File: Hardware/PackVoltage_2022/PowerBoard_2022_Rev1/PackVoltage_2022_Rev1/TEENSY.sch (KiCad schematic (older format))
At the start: 8 parts

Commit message: Back to TEENSY
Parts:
- removed U? (x8): TM4C129E_Launchpad, symbol MRDT_Shields:TM4C129E_Launchpad
- added U?: Teensy4.1_DEV-16771, MODULE_DEV-16771, symbol MRDT_Shields:Teensy4.1_DEV-16771
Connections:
- net labels added: Current_Sensor_Spare
- net labels removed: Current_Sensor_AuxAct, Current_Sensor_AuxLog, Current_Sensor_BBB, Current_Sensor_Cam1, Current_Sensor_Cam2, Current_Sensor_Drive, Current_Sensor_GimAct, Current_Sensor_GimLog, Current_Sensor_Multi, Current_Sensor_Nav, Current_Sensor_NetSwitch, Current_Sensor_SciAct, Driver_AuxAct, Driver_AuxLog, Driver_BBB, Driver_Cam1, Driver_Cam2, Driver_Drive, Driver_GimAct, Driver_Multi, Driver_Nav, Driver_NetSwitch, Driver_SciAct, Driver_SciLog
- wire segments 43 -> 22
- no-connect marks 34 -> 38

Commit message: Organizing stuff
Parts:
- U19: renamed from U?; footprint MODULE_DEV-16771 -> MRDT_Shields:MODULE_DEV-16771
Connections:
- no-connect marks 38 -> 39
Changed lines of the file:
@@
 Current_Sensor_M5
 $Comp
-L MRDT_Shields:Teensy4.1_DEV-16771 U?
+L MRDT_Shields:Teensy4.1_DEV-16771 U19
 U 1 1 62368E05
 P 5600 3550
-F 0 "U?" H 5600 5717 50  0000 C CNN
+F 0 "U19" H 5600 5717 50  0000 C CNN
 F 1 "Teensy4.1_DEV-16771" H 5600 5626 50  0000 C CNN
-F 2 "MODULE_DEV-16771" H 7700 3250 50  0001 L BNN
+F 2 "MRDT_Shields:MODULE_DEV-16771" H 7700 3250 50  0001 L BNN
 F 3 "" H 5600 3550 50  0001 L BNN
 F 4 "Manufacturer recommendations" H 7700 3000 50  0001 L BNN "STANDARD"
@@
 	6550 1750 6550 1550
 $Comp
-L power:+3.3V #PWR?
+L power:+3.3V #PWR0144
 U 1 1 623850B6
 P 6550 1550
-F 0 "#PWR?" H 6550 1400 50  0001 C CNN
+F 0 "#PWR0144" H 6550 1400 50  0001 C CNN
 F 1 "+3.3V" H 6565 1723 50  0000 C CNN
 F 2 "" H 6550 1550 50  0001 C CNN
@@
 	6500 5450 6500 5550
 $Comp
-L power:GND #PWR?
+L power:GND #PWR0145
 U 1 1 623DD9ED
 P 6500 5550
-F 0 "#PWR?" H 6500 5300 50  0001 C CNN
+F 0 "#PWR0145" H 6500 5300 50  0001 C CNN
 F 1 "GND" H 6505 5377 50  0000 C CNN
 F 2 "" H 6500 5550 50  0001 C CNN
@@
 	1    0    0    -1
 $EndComp
+NoConn ~ 6400 1650
 $EndSCHEMATC

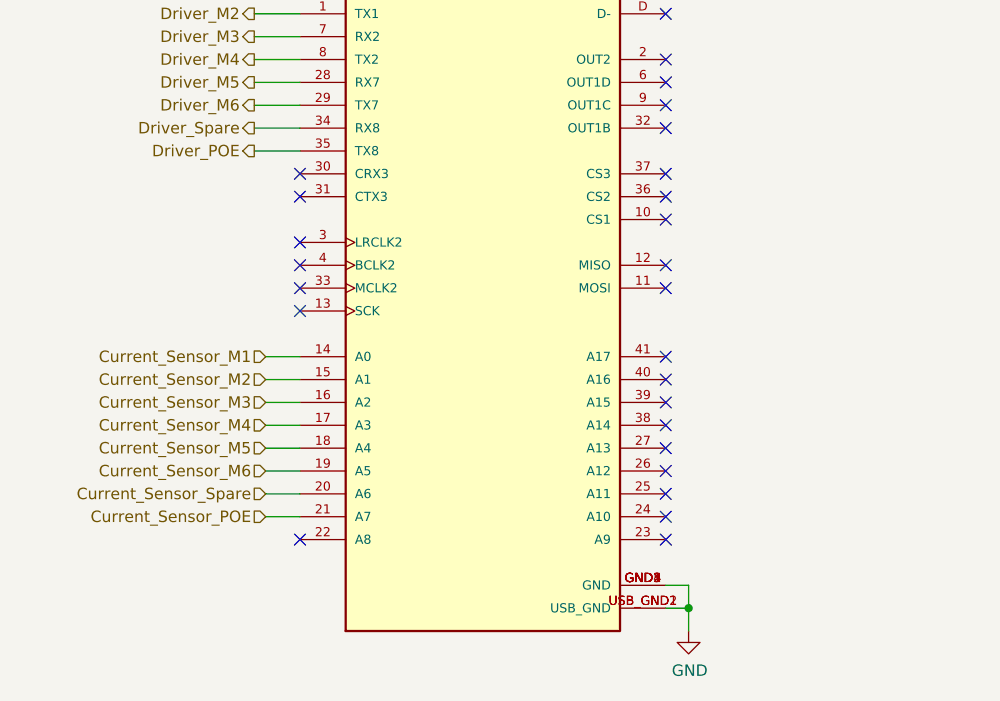
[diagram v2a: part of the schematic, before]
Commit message: added molex and fixed teensy
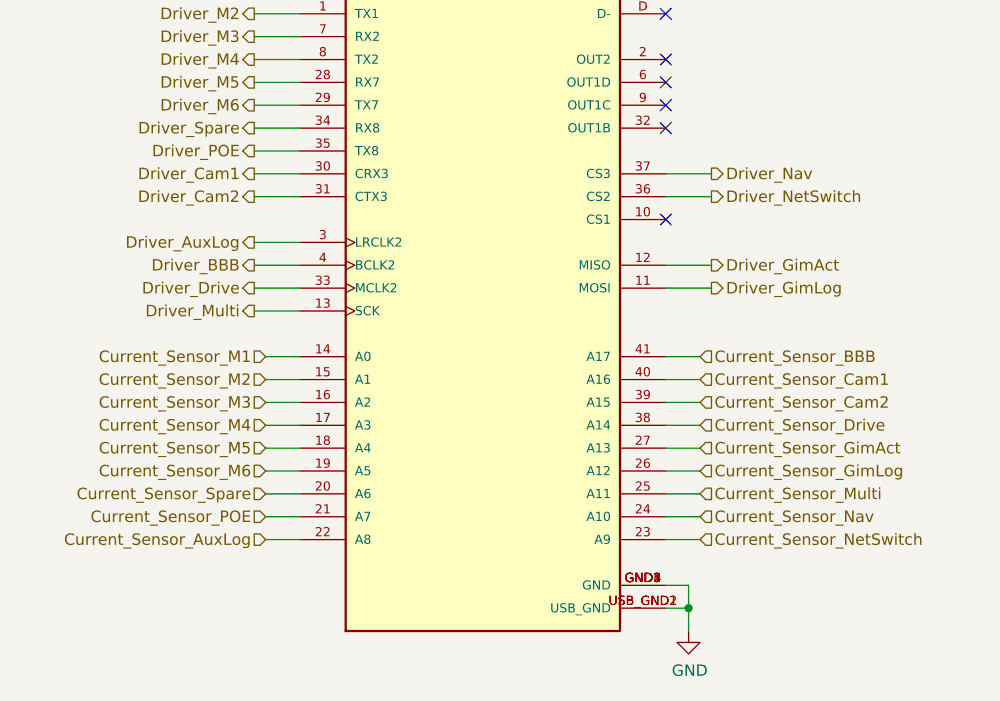
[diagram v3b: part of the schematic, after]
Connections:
- net Driver_GimLog: now reaches U19.11 (MOSI)
- net Driver_GimAct: now reaches U19.12 (MISO)
- net Driver_Multi: now reaches U19.13 (SCK)
- net Current_Sensor_AuxLog: now reaches U19.22 (A8)
- net Current_Sensor_NetSwitch: now reaches U19.23 (A9)
- net Current_Sensor_Nav: now reaches U19.24 (A10)
- net Current_Sensor_Multi: now reaches U19.25 (A11)
- net Current_Sensor_GimLog: now reaches U19.26 (A12)
- net Current_Sensor_GimAct: now reaches U19.27 (A13)
- net Driver_AuxLog: now reaches U19.3 (LRCLK2)
- net Driver_Cam1: now reaches U19.30 (CRX3)
- net Driver_Cam2: now reaches U19.31 (CTX3)
- net Driver_Drive: now reaches U19.33 (MCLK2)
- net Driver_NetSwitch: now reaches U19.36 (CS2)
- net Driver_Nav: now reaches U19.37 (CS3)
- net Current_Sensor_Drive: now reaches U19.38 (A14)
- net Current_Sensor_Cam2: now reaches U19.39 (A15)
- net Driver_BBB: now reaches U19.4 (BCLK2)
- net Current_Sensor_Cam1: now reaches U19.40 (A16)
- net Current_Sensor_BBB: now reaches U19.41 (A17)
- no-connect marks 39 -> 19
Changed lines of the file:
@@
 	1    0    0    -1
 $EndComp
-NoConn ~ 4800 5150
-NoConn ~ 6400 5150
-NoConn ~ 6400 5050
-NoConn ~ 6400 4950
-NoConn ~ 6400 4850
-NoConn ~ 6400 4750
-NoConn ~ 6400 4650
-NoConn ~ 6400 4550
-NoConn ~ 6400 4450
-NoConn ~ 6400 4350
-NoConn ~ 6400 4050
-NoConn ~ 6400 3950
-NoConn ~ 6400 3750
-NoConn ~ 6400 3650
-NoConn ~ 6400 3550
 NoConn ~ 6400 3350
 NoConn ~ 6400 3250
@@
 Wire Wire Line
 	4600 3450 4800 3450
-NoConn ~ 4800 3550
-NoConn ~ 4800 3650
-NoConn ~ 4800 3850
-NoConn ~ 4800 3950
-NoConn ~ 4800 4050
-NoConn ~ 4800 4150
 Wire Wire Line
 	6400 5350 6500 5350
@@
 $EndComp
 NoConn ~ 6400 1650
+Text HLabel 4650 5150 0    50   Input ~ 0
+Current_Sensor_AuxLog
+Wire Wire Line
+	4650 5150 4800 5150
+Text HLabel 6550 4350 2    50   Input ~ 0
+Current_Sensor_BBB
+Wire Wire Line
+	6550 4350 6400 4350
+Text HLabel 6550 4450 2    50   Input ~ 0
+Current_Sensor_Cam1
+Wire Wire Line
+	6550 4450 6400 4450
+Text HLabel 6550 4550 2    50   Input ~ 0
+Current_Sensor_Cam2
+Wire Wire Line
+	6550 4550 6400 4550
+Text HLabel 6550 4650 2    50   Input ~ 0
+Current_Sensor_Drive
+Wire Wire Line
+	6550 4650 6400 4650
+Text HLabel 6550 4750 2    50   Input ~ 0
+Current_Sensor_GimAct
+Wire Wire Line
+	6550 4750 6400 4750
+Text HLabel 6550 4850 2    50   Input ~ 0
+Current_Sensor_GimLog
+Wire Wire Line
+	6550 4850 6400 4850
+Text HLabel 6550 4950 2    50   Input ~ 0
+Current_Sensor_Multi
+Wire Wire Line
+	6550 4950 6400 4950
+Text HLabel 6550 5050 2    50   Input ~ 0
+Current_Sensor_Nav
+Wire Wire Line
+	6550 5050 6400 5050
+Text HLabel 6550 5150 2    50   Input ~ 0
+Current_Sensor_NetSwitch
+Wire Wire Line
+	6550 5150 6400 5150
+Text HLabel 4600 3550 0    50   Output ~ 0
+Driver_Cam1
+Wire Wire Line
+	4600 3550 4800 3550
+Text HLabel 4600 3650 0    50   Output ~ 0
+Driver_Cam2
+Wire Wire Line
+	4600 3650 4800 3650
+Text HLabel 4600 3850 0    50   Output ~ 0
+Driver_AuxLog
+Wire Wire Line
+	4600 3850 4800 3850
+Text HLabel 4600 3950 0    50   Output ~ 0
+Driver_BBB
+Wire Wire Line
+	4600 3950 4800 3950
+Text HLabel 4600 4050 0    50   Output ~ 0
+Driver_Drive
+Wire Wire Line
+	4600 4050 4800 4050
+Text HLabel 4600 4150 0    50   Output ~ 0
+Driver_Multi
+Wire Wire Line
+	4600 4150 4800 4150
+Text HLabel 6600 3950 2    50   Output ~ 0
+Driver_GimAct
+Wire Wire Line
+	6600 3950 6400 3950
+Text HLabel 6600 4050 2    50   Output ~ 0
+Driver_GimLog
+Wire Wire Line
+	6600 4050 6400 4050
+Text HLabel 6600 3550 2    50   Output ~ 0
+Driver_Nav
+Wire Wire Line
+	6600 3550 6400 3550
+Text HLabel 6600 3650 2    50   Output ~ 0
+Driver_NetSwitch
+Wire Wire Line
+	6600 3650 6400 3650
+NoConn ~ 6400 3750
 $EndSCHEMATC

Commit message: Somewhat completed schematic
did stuff
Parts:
- added C?: 0.1 uF, symbol Device:CP1
- added Conn?: Molex_uF_D_06, MRDT_Connectors:MOLEX_uF_D_06_Horizontal, symbol MRDT_Connectors:Molex_uF_D_06
- added J?: RJ45_LED_Shielded, symbol Connector:RJ45_LED_Shielded
- U19: symbol MRDT_Shields:Teensy4.1_DEV-16771 -> PackVoltage_2022_Rev1-rescue:Teensy4.1_DEV-16771-MRDT_Shields
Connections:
- net Current_Sensor_GimAct is gone; now on net Current_Sensor_Drive: U19.27 (A13)
- net Current_Sensor_BBB: now also U19.40 (A16); no longer U19.41 (A17)
- net Current_Sensor_Cam1: now also U19.39 (A15); no longer U19.40 (A16)
- net Current_Sensor_Cam2: now also U19.38 (A14); no longer U19.39 (A15)
- net Current_Sensor_Drive: no longer U19.38 (A14)
- net GND: now also J?.SH
- net Driver_AuxAct: now reaches U19.10 (CS1)
- net Current_Sensor_GimLog renamed Current_Sensor_Gim
- net Driver_GimAct: no longer names the net of U19.12 (MISO)
- net Driver_GimLog renamed Driver_Gim
- new net: Conn?.1, J?.1
- new net: Conn?.4, J?.10
- new net: C?.1, J?.2, J?.5
- new net: Conn?.2, J?.3
- new net: Conn?.6, J?.4
- new net: Conn?.5, J?.6
- new net: C?.2, Conn?.3, J?.8, J?.9
- new net Current_Sensor_AuxAct: U19.41 (A17)
- no-connect marks 19 -> 22
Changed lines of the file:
@@
 Current_Sensor_M5
 $Comp
-L MRDT_Shields:Teensy4.1_DEV-16771 U19
+L PackVoltage_2022_Rev1-rescue:Teensy4.1_DEV-16771-MRDT_Shields U19
 U 1 1 62368E05
 P 5600 3550
@@
 NoConn ~ 6400 2850
 NoConn ~ 6400 2750
-NoConn ~ 6400 2550
-NoConn ~ 6400 2450
-NoConn ~ 6400 2350
-NoConn ~ 6400 2250
-NoConn ~ 6400 2150
 NoConn ~ 6400 1850
 NoConn ~ 6400 1950
@@
 Wire Wire Line
 	4650 5150 4800 5150
-Text HLabel 6550 4350 2    50   Input ~ 0
+Text HLabel 6550 4450 2    50   Input ~ 0
 Current_Sensor_BBB
 Wire Wire Line
 	6550 4350 6400 4350
-Text HLabel 6550 4450 2    50   Input ~ 0
+Text HLabel 6550 4550 2    50   Input ~ 0
 Current_Sensor_Cam1
 Wire Wire Line
 	6550 4450 6400 4450
-Text HLabel 6550 4550 2    50   Input ~ 0
+Text HLabel 6550 4650 2    50   Input ~ 0
 Current_Sensor_Cam2
 Wire Wire Line
 	6550 4550 6400 4550
-Text HLabel 6550 4650 2    50   Input ~ 0
+Text HLabel 6550 4750 2    50   Input ~ 0
 Current_Sensor_Drive
 Wire Wire Line
 	6550 4650 6400 4650
-Text HLabel 6550 4750 2    50   Input ~ 0
-Current_Sensor_GimAct
-Wire Wire Line
-	6550 4750 6400 4750
 Text HLabel 6550 4850 2    50   Input ~ 0
-Current_Sensor_GimLog
+Current_Sensor_Gim
 Wire Wire Line
 	6550 4850 6400 4850
@@
 Wire Wire Line
 	4600 4150 4800 4150
-Text HLabel 6600 3950 2    50   Output ~ 0
-Driver_GimAct
-Wire Wire Line
-	6600 3950 6400 3950
 Text HLabel 6600 4050 2    50   Output ~ 0
-Driver_GimLog
+Driver_Gim
 Wire Wire Line
 	6600 4050 6400 4050
@@
 Wire Wire Line
 	6600 3650 6400 3650
-NoConn ~ 6400 3750
+NoConn ~ 6400 3950
+NoConn ~ 6400 2150
+NoConn ~ 6400 2250
+NoConn ~ 6400 2350
+NoConn ~ 6400 2450
+NoConn ~ 6400 2550
+$Comp
+L Connector:RJ45_LED_Shielded J?
+U 1 1 623B0B29
+P 9400 3050
+F 0 "J?" H 9400 3717 50  0000 C CNN
+F 1 "RJ45_LED_Shielded" H 9400 3626 50  0000 C CNN
+F 2 "" V 9400 3075 50  0001 C CNN
+F 3 "~" V 9400 3075 50  0001 C CNN
+	1    9400 3050
+	0    1    1    0
+$EndComp
+$Comp
+L MRDT_Connectors:Molex_uF_D_06 Conn?
+U 1 1 623B4892
+P 9850 4200
+F 0 "Conn?" V 9739 4372 60  0000 R CNN
+F 1 "Molex_uF_D_06" V 9845 4372 60  0000 R CNN
+F 2 "MRDT_Connectors:MOLEX_uF_D_06_Horizontal" H 9850 4500 60  0001 C CNN
+F 3 "" H 9850 4500 60  0001 C CNN
+	1    9850 4200
+	0    -1   1    0
+$EndComp
+Wire Wire Line
+	9100 4000 9100 3450
+Wire Wire Line
+	9200 4000 9200 3750
+Wire Wire Line
+	9200 3750 9300 3750
+Wire Wire Line
+	9300 3750 9300 3450
+Wire Wire Line
+	9600 4000 9600 3800
+Wire Wire Line
+	9600 3800 9400 3800
+Wire Wire Line
+	9400 3800 9400 3450
+Wire Wire Line
+	9500 4000 9500 3750
+Wire Wire Line
+	9500 3750 9600 3750
+Wire Wire Line
+	9600 3750 9600 3450
+Wire Wire Line
+	9400 4000 9400 3850
+Wire Wire Line
+	9400 3850 8700 3850
+Wire Wire Line
+	8700 3850 8700 2450
+Wire Wire Line
+	8700 2450 9700 2450
+Wire Wire Line
+	9700 2450 9700 2650
+Wire Wire Line
+	8900 3050 8550 3050
+Wire Wire Line
+	8550 3050 8550 3150
+$Comp
+L power:GND #PWR?
+U 1 1 623BDF76
+P 8550 3150
+F 0 "#PWR?" H 8550 2900 50  0001 C CNN
+F 1 "GND" H 8555 2977 50  0000 C CNN
+F 2 "" H 8550 3150 50  0001 C CNN
+F 3 "" H 8550 3150 50  0001 C CNN
+	1    8550 3150
+	1    0    0    -1
+$EndComp
+Wire Wire Line
+	9800 2650 9800 2450
+Wire Wire Line
+	9800 2450 10200 2450
+Wire Wire Line
+	10200 2450 10200 3450
+Wire Wire Line
+	10200 3450 9800 3450
+Wire Wire Line
+	10200 3450 10200 3950
+Wire Wire Line
+	10200 3950 9300 3950
+Wire Wire Line
+	9300 3950 9300 4000
+Connection ~ 10200 3450
+Wire Wire Line
+	9200 3450 9200 3600
+Wire Wire Line
+	9200 3600 9500 3600
+Wire Wire Line
+	9500 3450 9500 3600
+Wire Wire Line
+	9500 3600 10500 3600
+Connection ~ 9500 3600
+Wire Wire Line
+	10200 3950 10500 3950
+Connection ~ 10200 3950
+$Comp
+L Device:CP1 C?
+U 1 1 623C74FB
+P 10500 3750
+F 0 "C?" H 10615 3796 50  0000 L CNN
+F 1 "0.1 uF" H 10615 3705 50  0000 L CNN
+F 2 "" H 10500 3750 50  0001 C CNN
+F 3 "~" H 10500 3750 50  0001 C CNN
+	1    10500 3750
+	1    0    0    -1
+$EndComp
+Wire Wire Line
+	10500 3950 10500 3900
+NoConn ~ 9100 2650
+NoConn ~ 9200 2650
+NoConn ~ 9700 3450
+Text HLabel 6550 4350 2    50   Input ~ 0
+Current_Sensor_AuxAct
+Wire Wire Line
+	6400 4750 6550 4750
+Text HLabel 6600 3750 2    50   Output ~ 0
+Driver_AuxAct
+Wire Wire Line
+	6400 3750 6600 3750
 $EndSCHEMATC

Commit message: Organized the board and started placing components in their locations
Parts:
- C27: renamed from C?; footprint (none) -> Capacitor_SMD:C_0603_1608Metric_Pad1.08x0.95mm_HandSolder
- Conn12: renamed from Conn?; symbol MRDT_Connectors:Molex_uF_D_06 -> PackVoltage_2022_Rev1-rescue:Molex_uF_D_06-MRDT_Connectors
- J1: renamed from J?; footprint (none) -> MRDT_Connectors:RJ45_Teensy
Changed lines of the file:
@@
 NoConn ~ 6400 2550
 $Comp
-L Connector:RJ45_LED_Shielded J?
+L Connector:RJ45_LED_Shielded J1
 U 1 1 623B0B29
 P 9400 3050
-F 0 "J?" H 9400 3717 50  0000 C CNN
+F 0 "J1" H 9400 3717 50  0000 C CNN
 F 1 "RJ45_LED_Shielded" H 9400 3626 50  0000 C CNN
-F 2 "" V 9400 3075 50  0001 C CNN
+F 2 "MRDT_Connectors:RJ45_Teensy" V 9400 3075 50  0001 C CNN
 F 3 "~" V 9400 3075 50  0001 C CNN
 	1    9400 3050
@@
 $EndComp
 $Comp
-L MRDT_Connectors:Molex_uF_D_06 Conn?
+L PackVoltage_2022_Rev1-rescue:Molex_uF_D_06-MRDT_Connectors Conn?
 U 1 1 623B4892
 P 9850 4200
-F 0 "Conn?" V 9739 4372 60  0000 R CNN
+AR Path="/623B4892" Ref="Conn?"  Part="1"
+AR Path="/620F03FF/623B4892" Ref="Conn12"  Part="1"
+F 0 "Conn12" V 9739 4372 60  0000 R CNN
 F 1 "Molex_uF_D_06" V 9845 4372 60  0000 R CNN
 F 2 "MRDT_Connectors:MOLEX_uF_D_06_Horizontal" H 9850 4500 60  0001 C CNN
@@
 	8550 3050 8550 3150
 $Comp
-L power:GND #PWR?
+L power:GND #PWR0161
 U 1 1 623BDF76
 P 8550 3150
-F 0 "#PWR?" H 8550 2900 50  0001 C CNN
+F 0 "#PWR0161" H 8550 2900 50  0001 C CNN
 F 1 "GND" H 8555 2977 50  0000 C CNN
 F 2 "" H 8550 3150 50  0001 C CNN
@@
 Connection ~ 10200 3950
 $Comp
-L Device:CP1 C?
+L Device:CP1 C27
 U 1 1 623C74FB
 P 10500 3750
-F 0 "C?" H 10615 3796 50  0000 L CNN
+F 0 "C27" H 10615 3796 50  0000 L CNN
 F 1 "0.1 uF" H 10615 3705 50  0000 L CNN
-F 2 "" H 10500 3750 50  0001 C CNN
+F 2 "Capacitor_SMD:C_0603_1608Metric_Pad1.08x0.95mm_HandSolder" H 10500 3750 50  0001 C CNN
 F 3 "~" H 10500 3750 50  0001 C CNN
 	1    10500 3750

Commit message: fixed schematic issues - renamed ports, removed unnecessary ports, corrected footprint assignments; began layout - created circuits for most ports, most components placed
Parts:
- Conn13: renamed from Conn12; footprint MRDT_Connectors:MOLEX_uF_D_06_Horizontal -> Connector_PinSocket_2.00mm:PinSocket_2x03_P2.00mm_Vertical; symbol PackVoltage_2022_Rev1-rescue:Molex_uF_D_06-MRDT_Connectors -> MRDT_Connectors:Molex_uF_D_06
- U20: renamed from U19; symbol PackVoltage_2022_Rev1-rescue:Teensy4.1_DEV-16771-MRDT_Shields -> MRDT_Shields:Teensy4.1_DEV-16771
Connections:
- net Driver_NetSwitch is gone; now on net Driver_Spare: U20.36 (CS2)
- net Driver_Spare: no longer U20.34 (RX8)
- net Current_Sensor_AuxAct renamed Current_Sensor_Aux
- net Current_Sensor_AuxLog renamed Current_Sensor_12VSpare
- net Current_Sensor_NetSwitch: no longer names the net of U20.23 (A9)
- net Current_Sensor_Spare renamed Current_Sensor_SpareMotor
- net Driver_AuxAct renamed Driver_Aux
- net Driver_AuxLog renamed Driver_12VSpare
- new net Driver_SpareMotor: U20.34 (RX8)
- no-connect marks 22 -> 23
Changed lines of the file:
@@
 Driver_M6
 Text HLabel 4600 3350 0    50   Output ~ 0
-Driver_Spare
+Driver_SpareMotor
 Text HLabel 4650 5050 0    50   Input ~ 0
 Current_Sensor_POE
@@
 Current_Sensor_M5
 $Comp
-L PackVoltage_2022_Rev1-rescue:Teensy4.1_DEV-16771-MRDT_Shields U19
+L MRDT_Shields:Teensy4.1_DEV-16771 U20
 U 1 1 62368E05
 P 5600 3550
-F 0 "U19" H 5600 5717 50  0000 C CNN
+F 0 "U20" H 5600 5717 50  0000 C CNN
 F 1 "Teensy4.1_DEV-16771" H 5600 5626 50  0000 C CNN
 F 2 "MRDT_Shields:MODULE_DEV-16771" H 7700 3250 50  0001 L BNN
@@
 $EndComp
 Text HLabel 4650 4950 0    50   Input ~ 0
-Current_Sensor_Spare
+Current_Sensor_SpareMotor
 Wire Wire Line
 	4650 4350 4800 4350
@@
 	6550 1750 6550 1550
 $Comp
-L power:+3.3V #PWR0144
+L power:+3.3V #PWR064
 U 1 1 623850B6
 P 6550 1550
-F 0 "#PWR0144" H 6550 1400 50  0001 C CNN
+F 0 "#PWR064" H 6550 1400 50  0001 C CNN
 F 1 "+3.3V" H 6565 1723 50  0000 C CNN
 F 2 "" H 6550 1550 50  0001 C CNN
@@
 	1    0    0    -1
 $EndComp
-NoConn ~ 6400 3350
 NoConn ~ 6400 3250
 NoConn ~ 6400 3150
-NoConn ~ 6400 3050
 NoConn ~ 6400 2850
 NoConn ~ 6400 2750
@@
 	6500 5450 6500 5550
 $Comp
-L power:GND #PWR0145
+L power:GND #PWR063
 U 1 1 623DD9ED
 P 6500 5550
-F 0 "#PWR0145" H 6500 5300 50  0001 C CNN
+F 0 "#PWR063" H 6500 5300 50  0001 C CNN
 F 1 "GND" H 6505 5377 50  0000 C CNN
 F 2 "" H 6500 5550 50  0001 C CNN
@@
 NoConn ~ 6400 1650
 Text HLabel 4650 5150 0    50   Input ~ 0
-Current_Sensor_AuxLog
+Current_Sensor_12VSpare
 Wire Wire Line
 	4650 5150 4800 5150
@@
 Wire Wire Line
 	6550 5050 6400 5050
-Text HLabel 6550 5150 2    50   Input ~ 0
-Current_Sensor_NetSwitch
-Wire Wire Line
-	6550 5150 6400 5150
 Text HLabel 4600 3550 0    50   Output ~ 0
 Driver_Cam1
@@
 	4600 3650 4800 3650
 Text HLabel 4600 3850 0    50   Output ~ 0
-Driver_AuxLog
+Driver_12VSpare
 Wire Wire Line
 	4600 3850 4800 3850
@@
 Wire Wire Line
 	6600 3550 6400 3550
-Text HLabel 6600 3650 2    50   Output ~ 0
-Driver_NetSwitch
-Wire Wire Line
-	6600 3650 6400 3650
 NoConn ~ 6400 3950
 NoConn ~ 6400 2150
@@
 $EndComp
 $Comp
-L PackVoltage_2022_Rev1-rescue:Molex_uF_D_06-MRDT_Connectors Conn?
+L MRDT_Connectors:Molex_uF_D_06 Conn?
 U 1 1 623B4892
 P 9850 4200
 AR Path="/623B4892" Ref="Conn?"  Part="1"
-AR Path="/620F03FF/623B4892" Ref="Conn12"  Part="1"
-F 0 "Conn12" V 9739 4372 60  0000 R CNN
+AR Path="/620F03FF/623B4892" Ref="Conn13"  Part="1"
+F 0 "Conn13" V 9739 4372 60  0000 R CNN
 F 1 "Molex_uF_D_06" V 9845 4372 60  0000 R CNN
-F 2 "MRDT_Connectors:MOLEX_uF_D_06_Horizontal" H 9850 4500 60  0001 C CNN
+F 2 "Connector_PinSocket_2.00mm:PinSocket_2x03_P2.00mm_Vertical" H 9850 4500 60  0001 C CNN
 F 3 "" H 9850 4500 60  0001 C CNN
 	1    9850 4200
@@
 	8550 3050 8550 3150
 $Comp
-L power:GND #PWR0161
+L power:GND #PWR065
 U 1 1 623BDF76
 P 8550 3150
-F 0 "#PWR0161" H 8550 2900 50  0001 C CNN
+F 0 "#PWR065" H 8550 2900 50  0001 C CNN
 F 1 "GND" H 8555 2977 50  0000 C CNN
 F 2 "" H 8550 3150 50  0001 C CNN
@@
 NoConn ~ 9700 3450
 Text HLabel 6550 4350 2    50   Input ~ 0
-Current_Sensor_AuxAct
+Current_Sensor_Aux
 Wire Wire Line
 	6400 4750 6550 4750
 Text HLabel 6600 3750 2    50   Output ~ 0
-Driver_AuxAct
+Driver_Aux
 Wire Wire Line
 	6400 3750 6600 3750
+NoConn ~ 6400 3350
+Text HLabel 6600 3650 2    50   Output ~ 0
+Driver_Spare
+Wire Wire Line
+	6400 3650 6600 3650
+NoConn ~ 6400 5150
+NoConn ~ 6400 3050
 $EndSCHEMATC

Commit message: All connections made
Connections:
- net Current_Sensor_12VSpare: now also U20.27 (A13); no longer U20.22 (A8)
- net Current_Sensor_Aux: now also U20.18 (A4); no longer U20.41 (A17)
- net Current_Sensor_BBB: now also U20.17 (A3); no longer U20.40 (A16)
- net Current_Sensor_Cam1: now also U20.16 (A2); no longer U20.39 (A15)
- net Current_Sensor_Cam2: now also U20.15 (A1); no longer U20.38 (A14)
- net Current_Sensor_Drive: now also U20.14 (A0); no longer U20.27 (A13)
- net Current_Sensor_Gim: now also U20.24 (A10); no longer U20.26 (A12)
- net Current_Sensor_M1: now also U20.38 (A14); no longer U20.14 (A0)
- net Current_Sensor_M2: now also U20.39 (A15); no longer U20.15 (A1)
- net Current_Sensor_M3: now also U20.40 (A16); no longer U20.16 (A2)
- net Current_Sensor_M4: now also U20.41 (A17); no longer U20.17 (A3)
- net Current_Sensor_M5: now also U20.19 (A5); no longer U20.18 (A4)
- net Current_Sensor_M6: now also U20.20 (A6); no longer U20.19 (A5)
- net Current_Sensor_Nav: now also U20.26 (A12); no longer U20.24 (A10)
- net Current_Sensor_POE: now also U20.22 (A8); no longer U20.21 (A7)
- net Current_Sensor_SpareMotor: now also U20.21 (A7); no longer U20.20 (A6)
- net Driver_12VSpare: now also U20.0 (RX1); no longer U20.3 (LRCLK2)
- net Driver_Aux: now also U20.8 (TX2); no longer U20.10 (CS1)
- net Driver_BBB: now also U20.7 (RX2); no longer U20.4 (BCLK2)
- net Driver_Cam1: now also U20.6 (OUT1D); no longer U20.30 (CRX3)
- net Driver_Cam2: now also U20.5 (IN2); no longer U20.31 (CTX3)
- net Driver_Drive: now also U20.4 (BCLK2); no longer U20.33 (MCLK2)
- net Driver_Gim: now also U20.3 (LRCLK2); no longer U20.11 (MOSI)
- net Driver_M1: now also U20.33 (MCLK2); no longer U20.0 (RX1)
- net Driver_M2: now also U20.32 (OUT1B); no longer U20.1 (TX1)
- net Driver_M3: now also U20.34 (RX8); no longer U20.7 (RX2)
- net Driver_M4: now also U20.31 (CTX3); no longer U20.8 (TX2)
- net Driver_M5: now also U20.35 (TX8); no longer U20.28 (RX7)
- net Driver_M6: now also U20.30 (CRX3); no longer U20.29 (TX7)
- net Driver_Multi: now also U20.2 (OUT2); no longer U20.13 (SCK)
- net Driver_Nav: now also U20.1 (TX1); no longer U20.37 (CS3)
- net Driver_POE: now also U20.29 (TX7); no longer U20.35 (TX8)
- net Driver_Spare: now also U20.37 (CS3); no longer U20.36 (CS2)
- net Driver_SpareMotor: now also U20.36 (CS2); no longer U20.34 (RX8)
